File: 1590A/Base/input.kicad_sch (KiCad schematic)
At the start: 8 parts, among them Q201 LS844

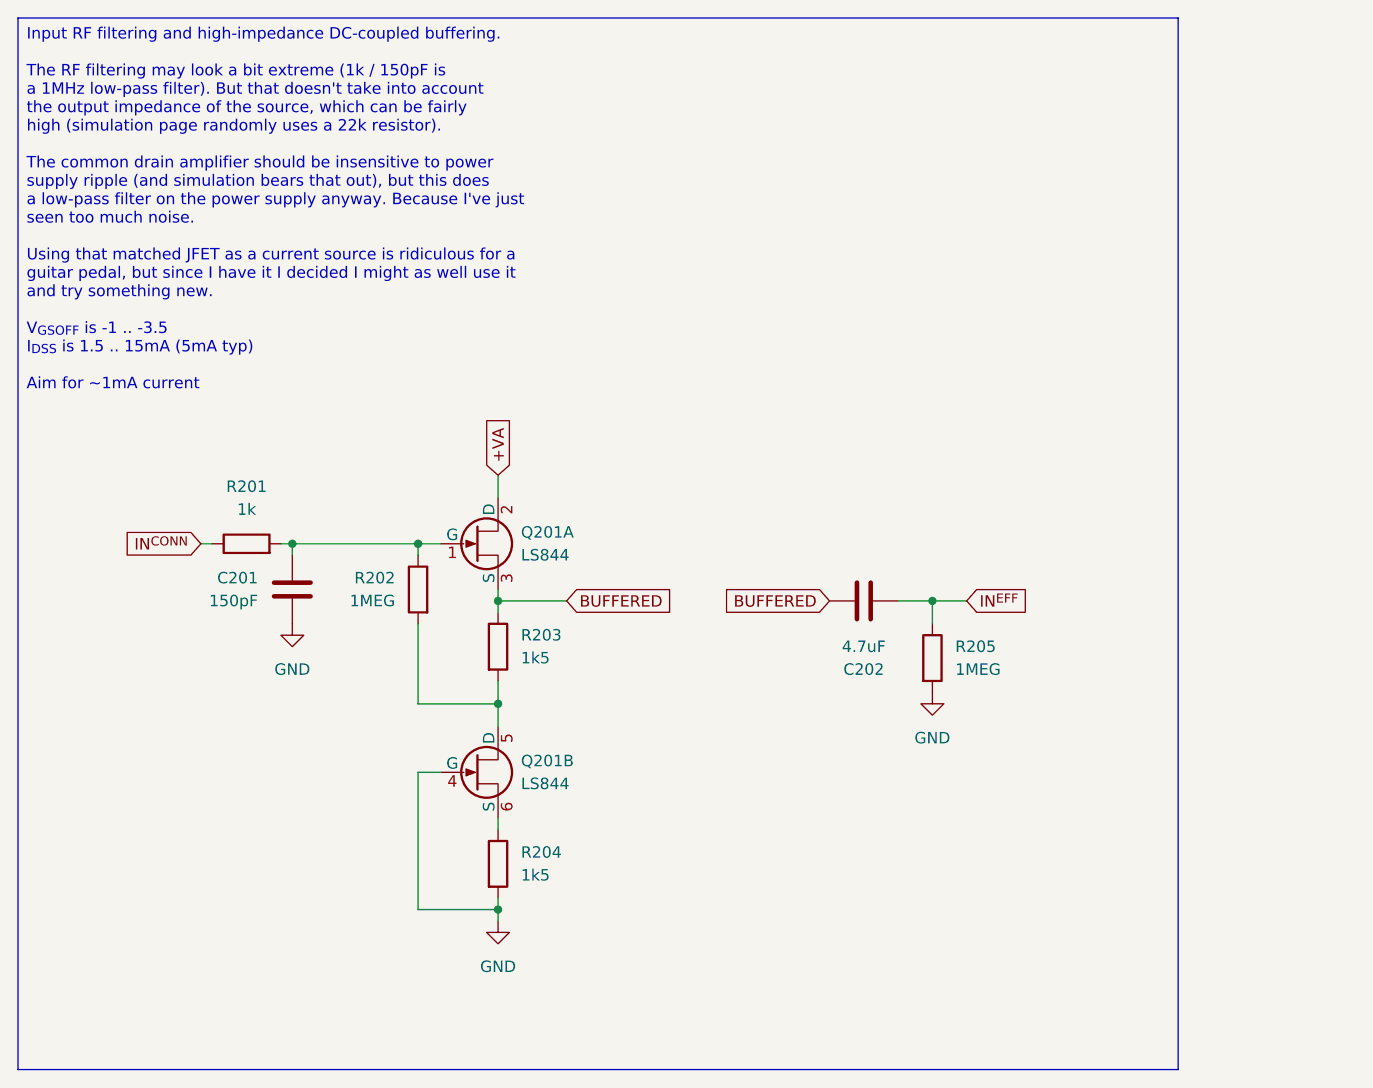
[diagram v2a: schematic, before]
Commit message: Don't DC-couple the LS844 JFET input
I didn't think this through: it looks superficially fine only because
the circuit doesn't make the _other_ side of the JFET gate connection
obvious.

Without the AC-coupling capacitor, the input gate of the LS844 now has a
relatively low impedance path to ground, going through the instrument.
So the self-biasing to ground with a high-value resistor doesn't work at
all.

To do DC coupling, I'd need an actual negative rail.  I technically knew
that, but I clearly hadn't really internalized it and so just overlooked
this obvious (in hindsight) fact entirely.

I do have the simulation infrastructure for this and when you look at
the results you see that the biasing is all wrong without the
DC-blocking capacitor in place.

But to see that you do need to look at it, and I hadn't bothered since
it all used to work fine and I didn't think about this.

Signed-off-by: Linus Torvalds <torvalds@linux-foundation.org>
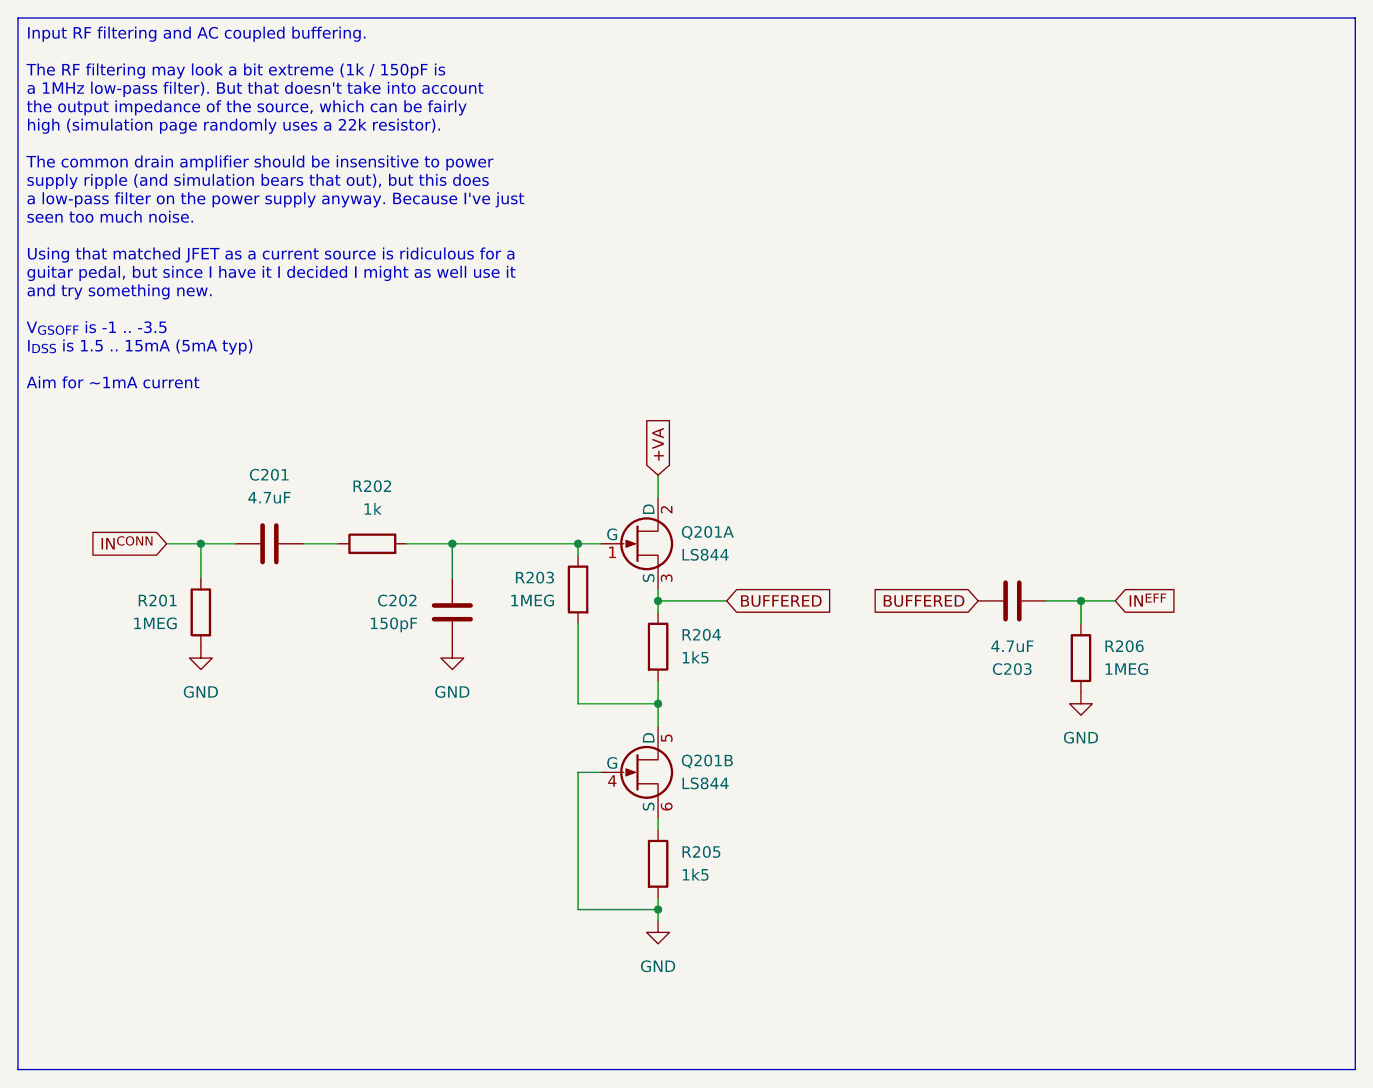
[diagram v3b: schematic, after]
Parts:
- added C201: 4.7uF, Capacitor_SMD:C_1206_3216Metric, symbol Device:C
- added R201: 1MEG, Resistor_SMD:R_0805_2012Metric, symbol Device:R
- renumbered C201 to C202, C202 to C203, R201 to R202, R202 to R203, R203 to R204, R204 to R205, R205 to R206
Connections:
- net GND: now also R201.2
- net IN^{CONN}: now also C201.1, R201.1; no longer R202.1
- new net: C201.2, R202.1
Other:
- moved on the sheet: C202, C203, Q201A, Q201B, R202, R203, R204, R205, R206
